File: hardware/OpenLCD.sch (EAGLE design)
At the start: 41 parts, among them Q1 PNP-500mA, Q2 PNP-500mA, Q3 PNP-500mA, U1 ATMEGA328P_TQFP, U2 4BIT-RGB, U3 MIC5205-ADJ, Y2 8MHz

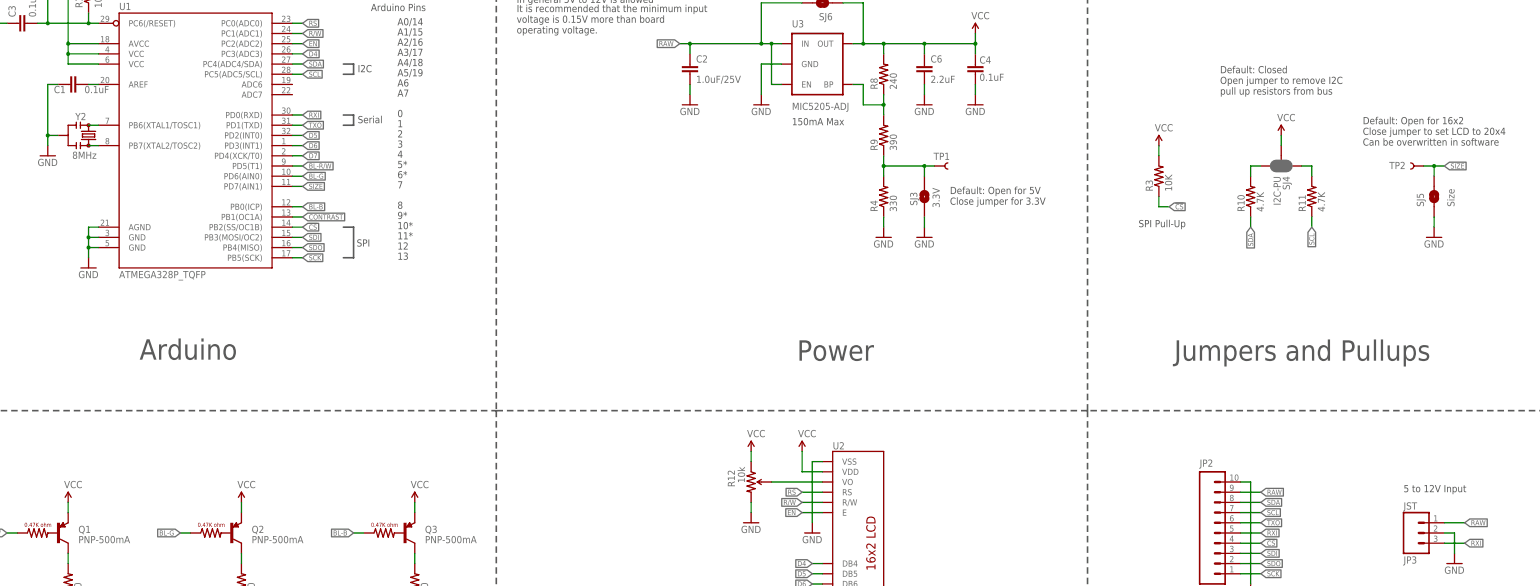
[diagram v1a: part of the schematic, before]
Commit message: Connected blue backlight control pin to PWM on ATmega
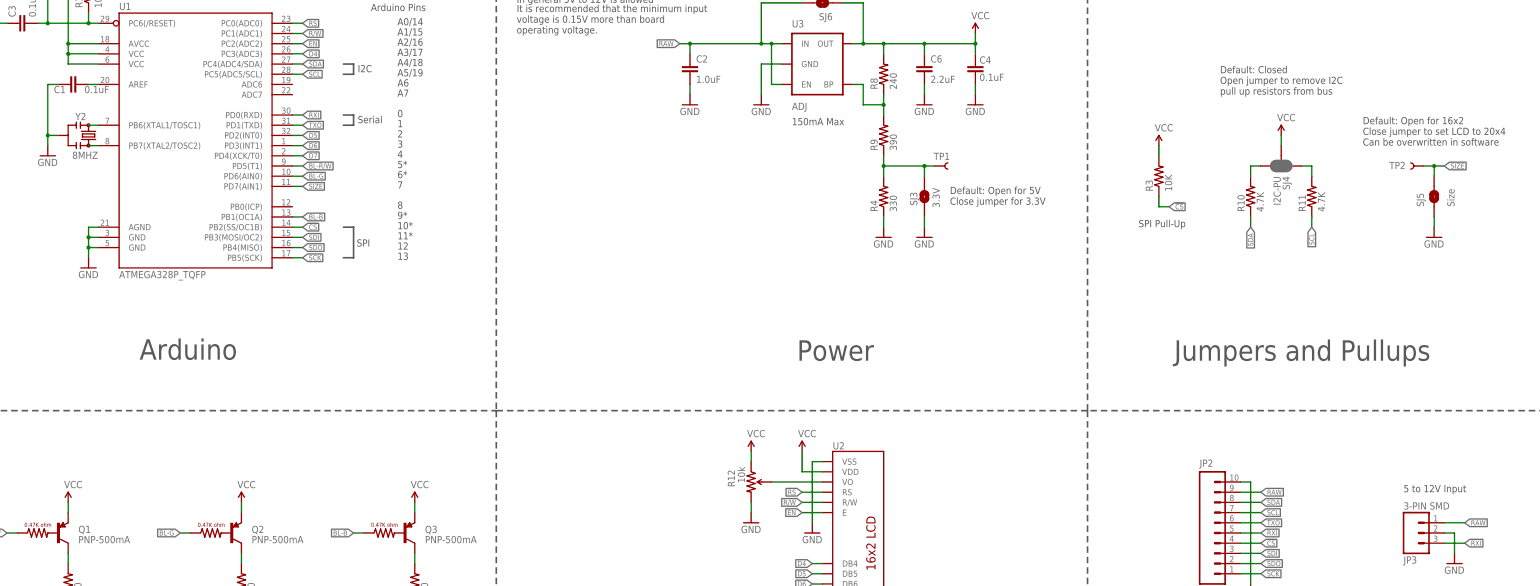
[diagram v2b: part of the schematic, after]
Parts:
- C2: value 1.0uF/25V -> 1.0uF; device SparkFun-Capacitors:1.0UF-25V-+80/-20(0805) -> SparkFun-Capacitors:1.0UF-25V-+80/-20(0805)"
- JP3: value JST -> 3-PIN SMD
- U3: value MIC5205-ADJ -> ADJ
- Y2: value 8MHz -> 8MHZ
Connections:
- removed net CONTRAST: U1.PB1(OC1A)
- net BL-B: now also U1.PB1(OC1A); no longer U1.PB0(ICP)
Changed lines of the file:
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@@
 <?xml version="1.0" encoding="utf-8"?>
 <!DOCTYPE eagle SYSTEM "eagle.dtd">
-<eagle version="7.3.0">
+<eagle version="7.2.0">
 <drawing>
 <settings>
@@
 <layer number="113" name="IDFDebug" color="7" fill="1" visible="yes" active="yes"/>
 <layer number="116" name="Patch_BOT" color="9" fill="4" visible="yes" active="yes"/>
+<layer number="118" name="Rect_Pads" color="7" fill="1" visible="yes" active="yes"/>
 <layer number="121" name="_tsilk" color="7" fill="1" visible="yes" active="yes"/>
 <layer number="122" name="_bsilk" color="7" fill="1" visible="yes" active="yes"/>
@@
 <part name="FID2" library="SparkFun-Aesthetics" deviceset="FIDUCIAL" device="1X2"/>
 <part name="GND4" library="SparkFun" deviceset="GND" device=""/>
-<part name="JP3" library="SparkFun-Connectors" deviceset="M03" device="JST-SMD" value="JST"/>
+<part name="JP3" library="SparkFun-Connectors" deviceset="M03" device="JST-SMD" value="3-PIN SMD"/>
 <part name="LOGO3" library="SparkFun-Aesthetics" deviceset="SFE_LOGO_NAME" device=".1_INCH"/>
 <part name="LOGO4" library="SparkFun-Aesthetics" deviceset="SFE_LOGO_FLAME" device=".1_STOP"/>
 <part name="U1" library="SparkFun-DigitalIC" deviceset="ATMEGA328P_TQFP" device="" value="ATMEGA328P_TQFP"/>
-<part name="Y2" library="SparkFun-FreqCtrl" deviceset="RESONATOR" device="8MHZ" value="8MHz"/>
+<part name="Y2" library="SparkFun-FreqCtrl" deviceset="RESONATOR" device="8MHZ" value="8MHZ"/>
 <part name="Q1" library="SparkFun-DiscreteSemi" deviceset="TRANSISTOR-PNP-DDTB142TC" device="" value="PNP-500mA"/>
 <part name="Q2" library="SparkFun-DiscreteSemi" deviceset="TRANSISTOR-PNP-DDTB142TC" device="" value="PNP-500mA"/>
@@
 <part name="GND5" library="SparkFun" deviceset="GND" device=""/>
 <part name="SJ5" library="SparkFun-Passives" deviceset="JUMPER-PAD-2-NO" device="YES_SILK" value="Size"/>
-<part name="U3" library="SparkFun-PowerIC" deviceset="V_REG_MIC5205" device="ADJ" value="MIC5205-ADJ"/>
+<part name="U3" library="SparkFun-PowerIC" deviceset="V_REG_MIC5205" device="ADJ" value="ADJ"/>
 <part name="R4" library="SparkFun-Resistors" deviceset="330OHM1/10W1%(0603)" device="" value="330"/>
 <part name="R8" library="SparkFun-Resistors" deviceset="240OHM1/10W1%(0603)" device="" value="240"/>
@@
 <part name="GND6" library="SparkFun" deviceset="GND" device=""/>
 <part name="GND8" library="SparkFun" deviceset="GND" device=""/>
-<part name="C2" library="SparkFun-Capacitors" deviceset="1.0UF-25V-+80/-20(0805)" device="" value="1.0uF/25V"/>
+<part name="C2" library="SparkFun-Capacitors" deviceset="1.0UF-25V-+80/-20(0805)" device="&quot;" value="1.0uF"/>
 <part name="C6" library="SparkFun-Capacitors" deviceset="2.2UF-10V-20%(0603)" device="" value="2.2uF"/>
 <part name="U2" library="SparkFun-Displays" deviceset="LCD-16X2-MIN" device="MIN4-RGB" value="4BIT-RGB"/>
@@
 </segment>
 <segment>
-<pinref part="U1" gate="U$1" pin="PB0(ICP)"/>
-<wire x1="114.3" y1="198.12" x2="116.84" y2="198.12" width="0.1524" layer="91"/>
-<label x="116.84" y="198.12" size="1.27" layer="95" xref="yes"/>
+<pinref part="U1" gate="U$1" pin="PB1(OC1A)"/>
+<wire x1="114.3" y1="195.58" x2="116.84" y2="195.58" width="0.1524" layer="91"/>
+<label x="116.84" y="195.58" size="1.27" layer="95" xref="yes"/>
 </segment>
 </net>
@@
 </segment>
 </net>
-<net name="CONTRAST" class="0">
-<segment>
-<wire x1="114.3" y1="195.58" x2="116.84" y2="195.58" width="0.1524" layer="91"/>
-<label x="116.84" y="195.58" size="1.27" layer="95" xref="yes"/>
-<pinref part="U1" gate="U$1" pin="PB1(OC1A)"/>
-</segment>
-</net>

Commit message: Added MCP4725 for contrast control. Changed to 10uF tantulum.
We're going to try using the internal band gap reference for temp
control and modify the contrast based on that temp. We'll see if it
works...
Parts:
- removed C6: 2.2uF, SparkFun-Capacitors:2.2UF-10V-20%(0603)
- removed R12: 10k, SparkFun-Electromechanical:TRIMPOTRES-09285
- added C5: 10uF, SparkFun-Capacitors:10UF-16V-10%(TANT)
- added U4: MCP4725, SparkFun-AnalogIC:MCP4725SOT-23
- C2: value 1.0uF -> 1.0uF/25V
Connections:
- net A-RED/WHITE renamed MONO/RED
- removed net 3.3V_CTRL: R4.2, R9.1, SJ3.2, TP1.1
- removed net N$8: R12.WIPER, U2.VO
- new net 3V-JUMPER: R4.2, R9.1, SJ3.2, TP1.1, U1.ADC6
- new net CONTRAST: U2.VO, U4.VOUT
- net GND: now also C5.-, U4.AO, U4.VSS; no longer C6.2, R12.CW
- net SCL: now also U4.SCL
- net SDA: now also U4.SDA
- net VCC: now also C5.+, U4.VDD; no longer C6.1, R12.CCW
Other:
- note added: "7-bit I2C address for ADC with A0 to GND = 0x60"
- note added: "Added connection to 3.3V jumper for thermo controlled contrast"
- note added: "Added warning text to bottom of LCD"
- note added: "Changed from 2.2uF ceramic to 10uF tantulum"
- note added: "Do not change the OpenLCD I2C address to 0x60 as this will conflict with the onboard DAC."
- note added: "Moved to MCP for contrast control"
- note added: "On RBG-backlit LCDs Backlight1 is Red cathode and Backlight2 is Red anode."
- note added: "On mono-backlit LCDs Backlight1 is anode and Backlight2 is cathode."
- note added: "On v02"
- note added: "Removed trimpot"
- note added: "TBD:"
- note added: "check what is displayed above 127"
- note added: "close 3,3v jumper by default?"
- note removed: "2 for I2C Address"
- note removed: "3 for backlight"
- note removed: "4 for SPI"
- note removed: "7 for LCD"
- note removed: "v1.0"
- moved on the sheet: U2

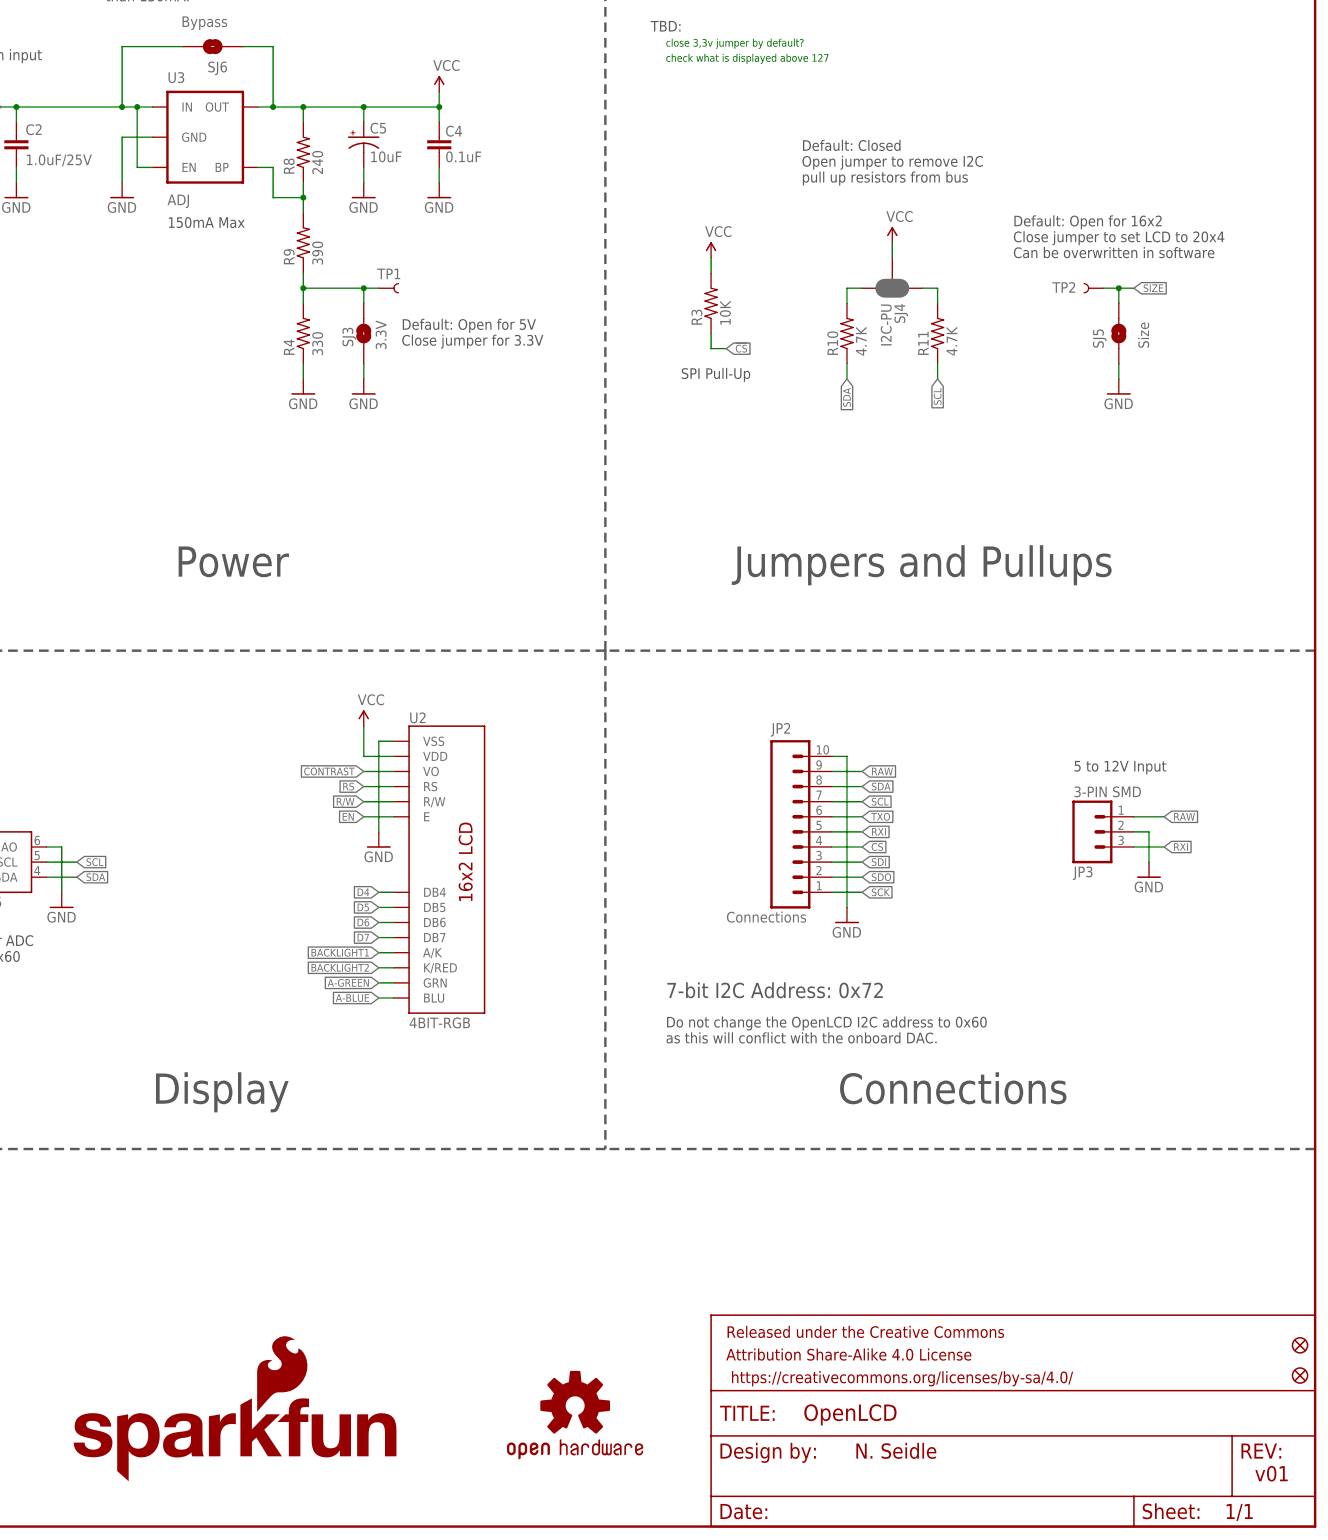
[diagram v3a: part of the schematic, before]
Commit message: Fixes for issue #4.
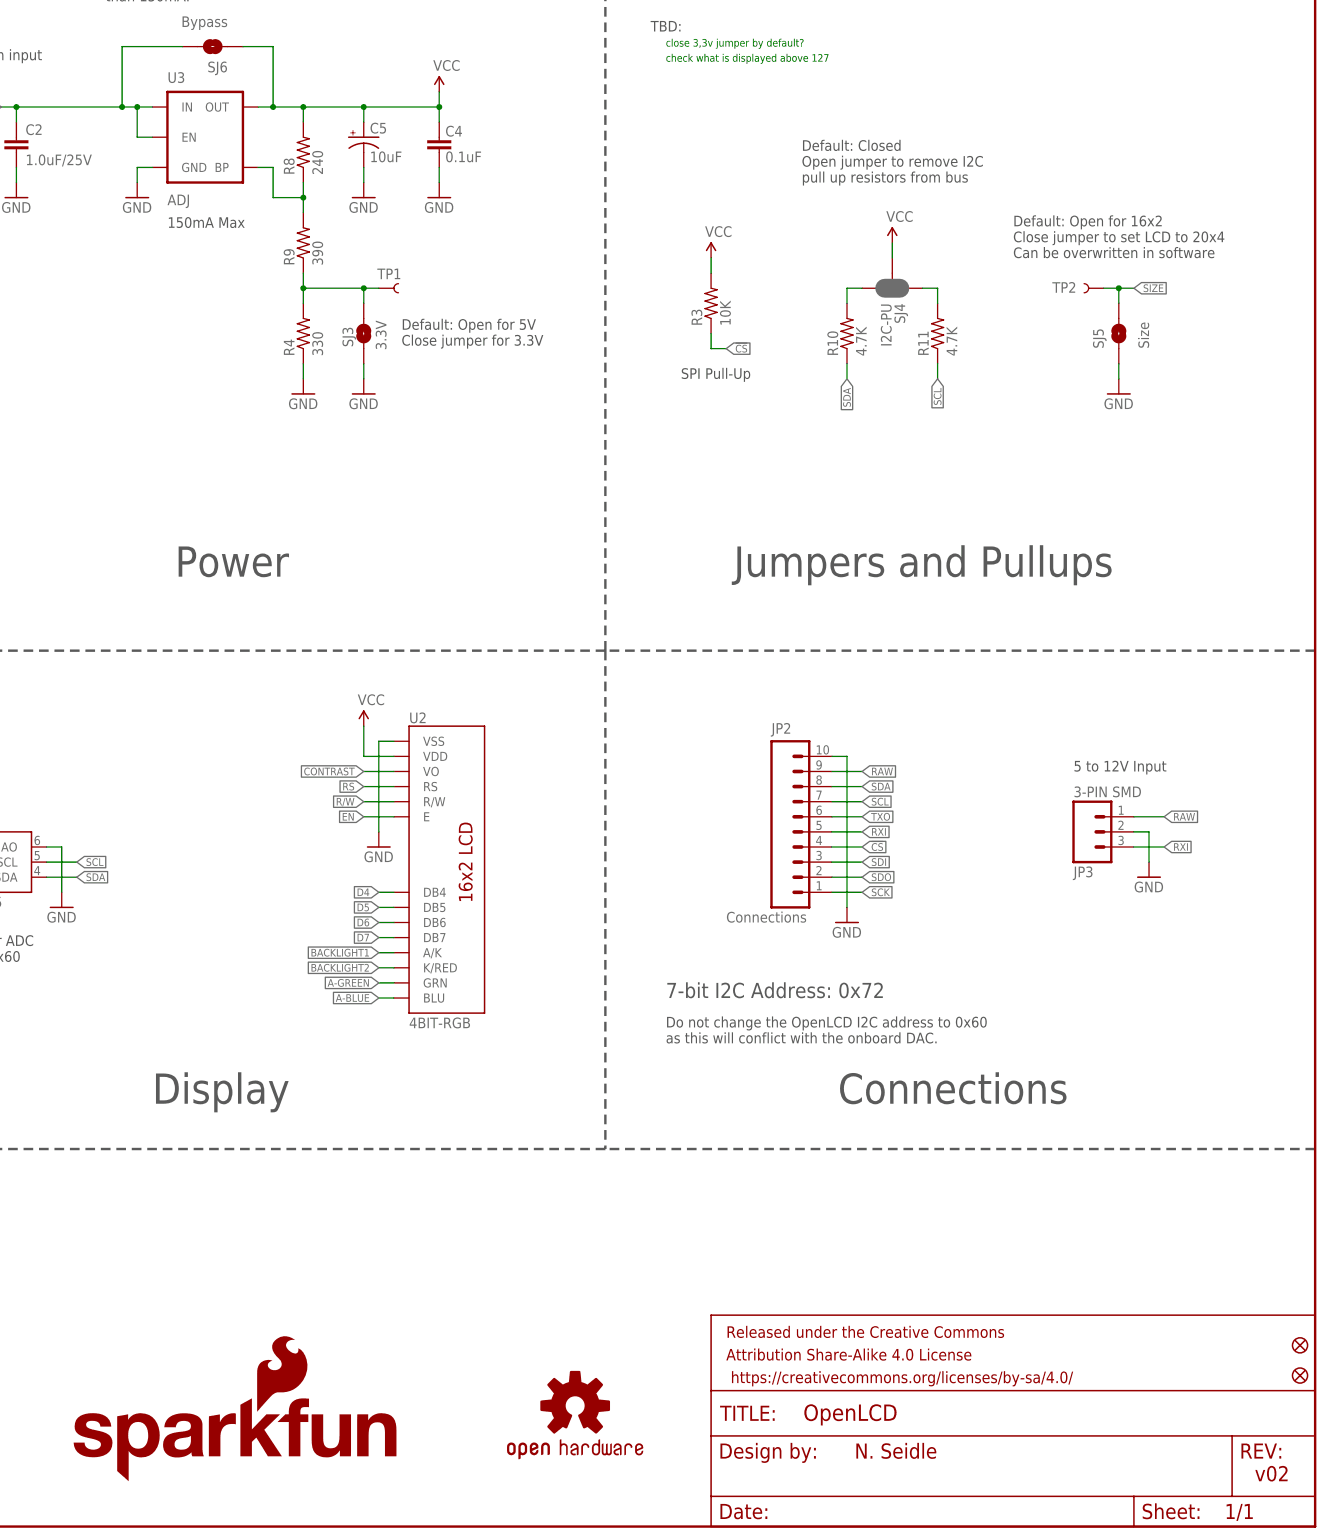
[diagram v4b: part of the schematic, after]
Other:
- note added: "v02"
- note removed: "v01"
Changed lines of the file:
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@@
 <layer number="112" name="tSilk" color="7" fill="1" visible="yes" active="yes"/>
 <layer number="113" name="IDFDebug" color="7" fill="1" visible="yes" active="yes"/>
+<layer number="114" name="Badge_Outline" color="7" fill="1" visible="yes" active="yes"/>
+<layer number="115" name="ReferenceISLANDS" color="7" fill="1" visible="yes" active="yes"/>
 <layer number="116" name="Patch_BOT" color="9" fill="4" visible="yes" active="yes"/>
 <layer number="118" name="Rect_Pads" color="7" fill="1" visible="yes" active="yes"/>
@@
 Can be overwritten in software</text>
 <text x="354.33" y="11.43" size="2.54" layer="94">N. Seidle</text>
-<text x="421.64" y="7.62" size="2.54" layer="94">v01</text>
+<text x="421.64" y="7.62" size="2.54" layer="94">v02</text>
 <text x="334.01" y="159.766" size="5.08" layer="97" ratio="15">Jumpers and Pullups</text>
 <text x="345.44" y="226.06" size="1.778" layer="97">Default: Closed
@@
 </instance>
 <instance part="GND1" gate="1" x="284.48" y="223.52"/>
-<instance part="GND30" gate="1" x="231.14" y="223.52"/>
+<instance part="GND30" gate="1" x="233.68" y="223.52"/>
 <instance part="GND32" gate="1" x="213.36" y="223.52"/>
 <instance part="GND16" gate="1" x="353.06" y="101.6"/>
@@
 </segment>
 <segment>
-<wire x1="236.22" y1="233.68" x2="231.14" y2="233.68" width="0.1524" layer="91"/>
-<wire x1="231.14" y1="233.68" x2="231.14" y2="226.06" width="0.1524" layer="91"/>
-<pinref part="GND30" gate="1" pin="GND"/>
-<pinref part="U3" gate="U1" pin="GND"/>
-</segment>
-<segment>
 <wire x1="213.36" y1="226.06" x2="213.36" y2="228.6" width="0.1524" layer="91"/>
 <pinref part="GND32" gate="1" pin="GND"/>
@@
 <pinref part="C5" gate="G$1" pin="-"/>
 <wire x1="271.78" y1="228.6" x2="271.78" y2="226.06" width="0.1524" layer="91"/>
+</segment>
+<segment>
+<pinref part="U3" gate="U1" pin="GND"/>
+<pinref part="GND30" gate="1" pin="GND"/>
+<wire x1="236.22" y1="228.6" x2="233.68" y2="228.6" width="0.1524" layer="91"/>
+<wire x1="233.68" y1="228.6" x2="233.68" y2="226.06" width="0.1524" layer="91"/>
 </segment>
 </net>
@@
 <net name="RAW" class="1">
 <segment>
-<wire x1="233.68" y1="238.76" x2="236.22" y2="238.76" width="0.1524" layer="91"/>
-<wire x1="236.22" y1="228.6" x2="233.68" y2="228.6" width="0.1524" layer="91"/>
-<wire x1="233.68" y1="228.6" x2="233.68" y2="238.76" width="0.1524" layer="91"/>
 <wire x1="213.36" y1="238.76" x2="231.14" y2="238.76" width="0.1524" layer="91"/>
 <wire x1="231.14" y1="238.76" x2="233.68" y2="238.76" width="0.1524" layer="91"/>
+<wire x1="233.68" y1="238.76" x2="236.22" y2="238.76" width="0.1524" layer="91"/>
 <wire x1="213.36" y1="236.22" x2="213.36" y2="238.76" width="0.1524" layer="91"/>
 <wire x1="213.36" y1="238.76" x2="210.82" y2="238.76" width="0.1524" layer="91"/>
-<junction x="233.68" y="238.76"/>
 <junction x="213.36" y="238.76"/>
 <label x="210.82" y="238.76" size="1.27" layer="95" rot="R180" xref="yes"/>
 <pinref part="U3" gate="U1" pin="IN"/>
-<pinref part="U3" gate="U1" pin="EN"/>
 <pinref part="C2" gate="G$1" pin="1"/>
 <pinref part="SJ6" gate="G$1" pin="2"/>
@@
 <wire x1="231.14" y1="248.92" x2="231.14" y2="238.76" width="0.1524" layer="91"/>
 <junction x="231.14" y="238.76"/>
-</segment>
-<segment>
+<pinref part="U3" gate="U1" pin="EN"/>
+<wire x1="236.22" y1="233.68" x2="233.68" y2="233.68" width="0.1524" layer="91"/>
+<wire x1="233.68" y1="233.68" x2="233.68" y2="238.76" width="0.1524" layer="91"/>
+<junction x="233.68" y="238.76"/>
+</segment>
+<segment>
